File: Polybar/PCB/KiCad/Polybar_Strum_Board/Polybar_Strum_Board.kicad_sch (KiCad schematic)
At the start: 25 parts, among them SW1 MX_SW_solder, SW2 MX_SW_solder, SW3 MX_SW_solder, SW4 MX_SW_HS, SW5 MX_SW_HS, U1 ProMicro, U2 RKJXV1224005

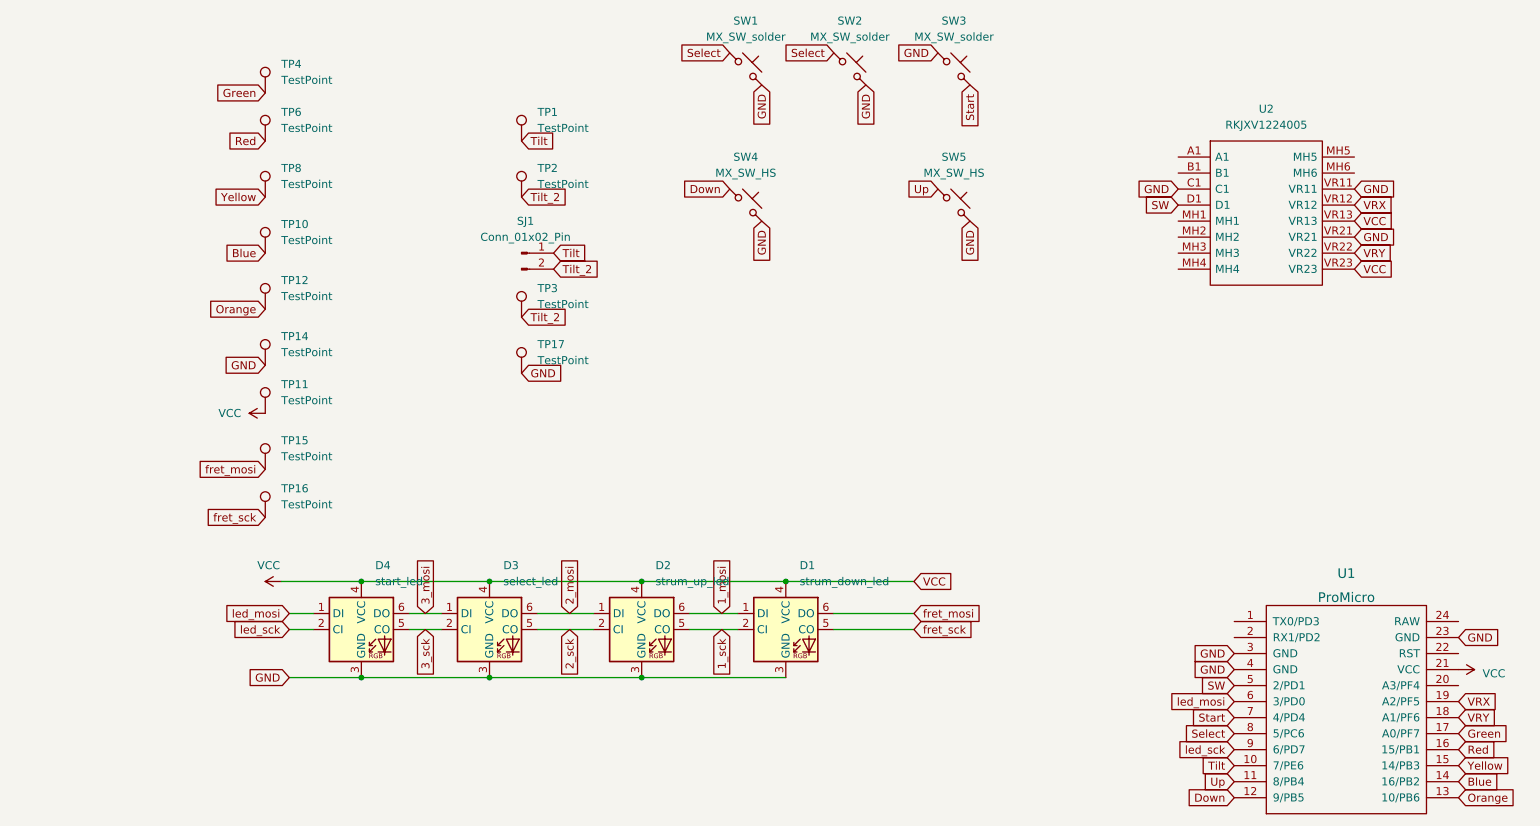
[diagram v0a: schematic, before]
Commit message: Switched connectors from test pins to an actual connector
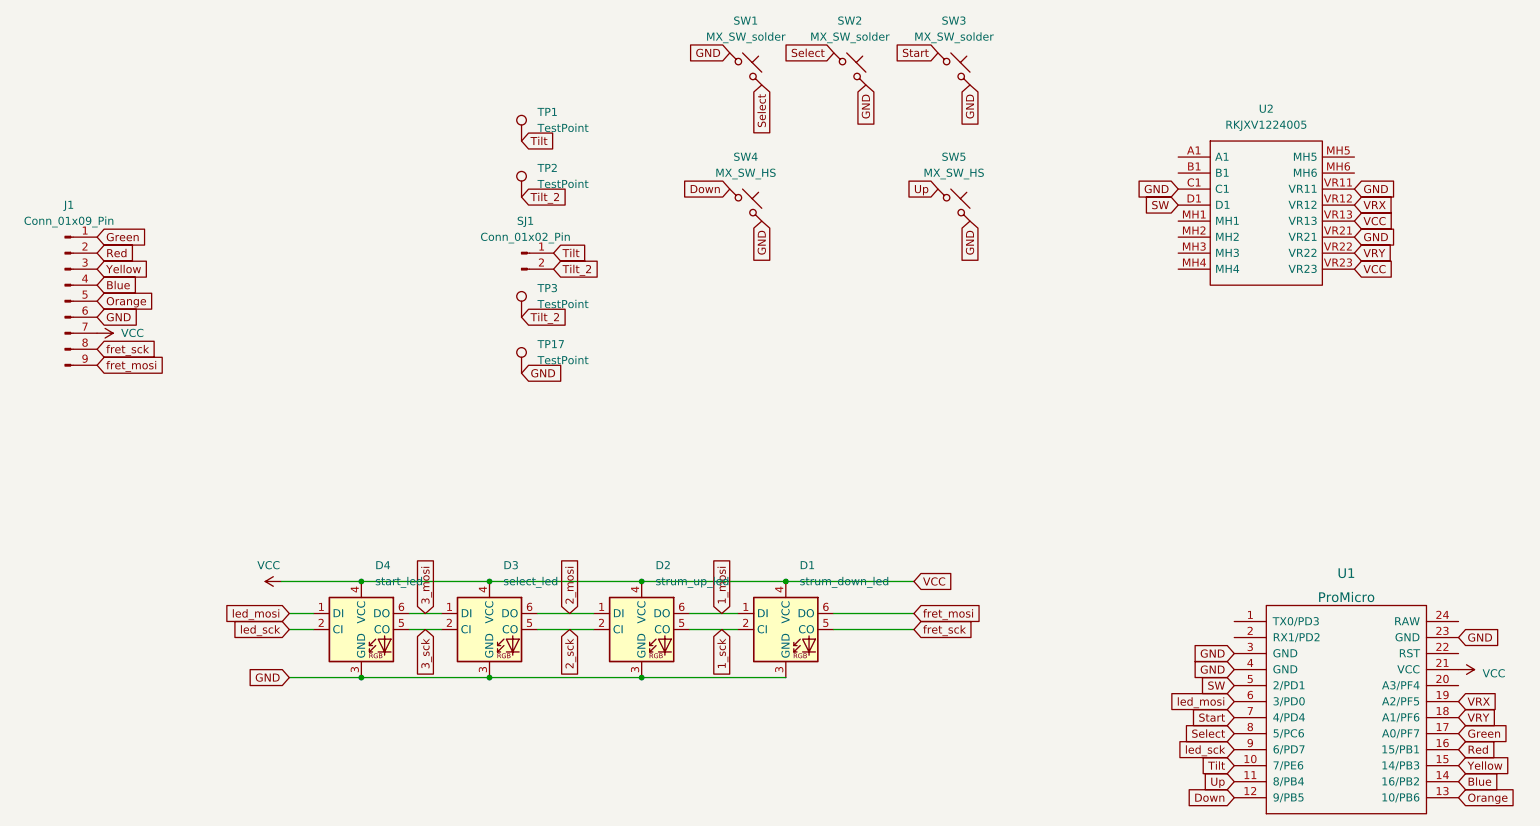
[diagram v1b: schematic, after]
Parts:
- removed TP10, TP11, TP12, TP14, TP15, TP16, TP4, TP6, TP8: TestPoint, Polybar:test_point, symbol Connector:TestPoint
- added J1: Conn_01x09_Pin, Connector_PinHeader_2.54mm:PinHeader_1x09_P2.54mm_Vertical, symbol Connector:Conn_01x09_Pin
- U2: footprint RKJXV1224005 -> Polybar:RKJXV1224005
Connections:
- net Blue: now also J1.4 (Pin_4)
- net GND: now also SW1.1, SW3.2, J1.6 (Pin_6); no longer SW1.2, SW3.1
- net Green: now also J1.1 (Pin_1)
- net Orange: now also J1.5 (Pin_5)
- net Red: now also J1.2 (Pin_2)
- net Select: now also SW1.2; no longer SW1.1
- net Start: now also SW3.1; no longer SW3.2
- net VCC: now also J1.7 (Pin_7)
- net Yellow: now also J1.3 (Pin_3)
- net fret_mosi: now also J1.9 (Pin_9)
- net fret_sck: now also J1.8 (Pin_8)

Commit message: re-routed pcb
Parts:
- removed TP1, TP17, TP2, TP3: TestPoint, Polybar:test_point_2, symbol Connector:TestPoint
- added SJ2, SJ3: Conn_01x02_Pin, Connector_PinHeader_2.54mm:PinHeader_1x02_P2.54mm_Vertical, symbol Connector:Conn_01x02_Pin
- U2: footprint Polybar:RKJXV1224005 -> RKJXV1224005
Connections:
- net 2_mosi: now also D1.6 (DO), D4.1 (DI); no longer D2.1 (DI), D3.6 (DO)
- net 2_sck: now also D1.5 (CO), D4.2 (CI); no longer D2.2 (CI), D3.5 (CO)
- net GND: now also U2.B2, SJ2.1 (Pin_1); no longer U2.C1
- net SW: now also U2.B1; no longer U2.D1
- net Tilt: now also SJ3.1 (Pin_1)
- net Tilt_2: now also SJ2.2 (Pin_2), SJ3.2 (Pin_2)
- net fret_mosi: now also D3.5 (CO); no longer D1.6 (DO)
- net fret_sck: now also D3.6 (DO); no longer D1.5 (CO)
- net led_mosi: now also D2.1 (DI); no longer D4.1 (DI)
- net led_sck: now also D2.2 (CI); no longer D4.2 (CI)
- new net SH: U2.SH
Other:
- title: (none) -> Polybar Strum Bar
- moved on the sheet: D1, D2, D3, D4
